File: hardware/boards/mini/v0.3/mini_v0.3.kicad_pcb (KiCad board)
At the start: 8 copper layers, 20 x 40 mm, 94 parts, among them IC1 NAU88C22YG, IC3 IS42S16160J-6BLI, J4 DF40C-90DP-0.4V, U1 W25Q128JVP, U2 LTV-217-G, U4 STM32H750XBHx, Y1 Crystal_GND24, Y3 32.768kHz

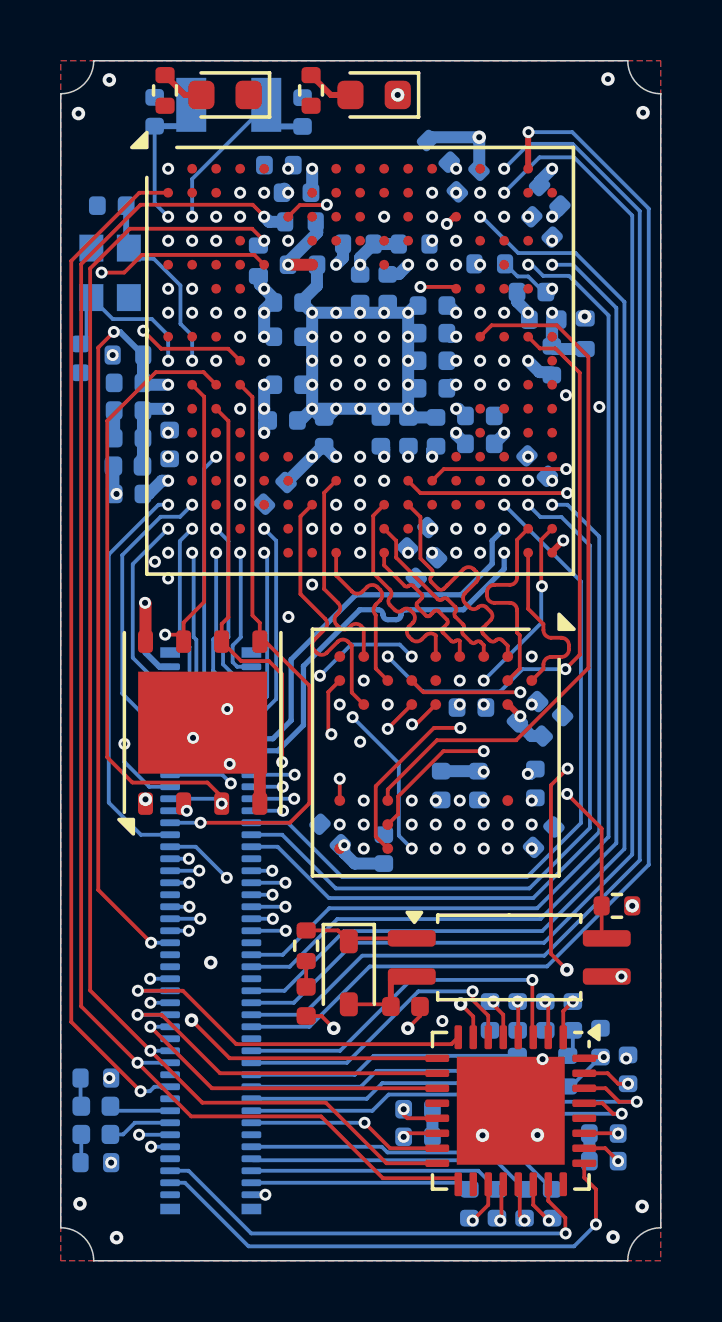
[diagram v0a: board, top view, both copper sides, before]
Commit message: mini: change flash to SOIC8 to fix routing
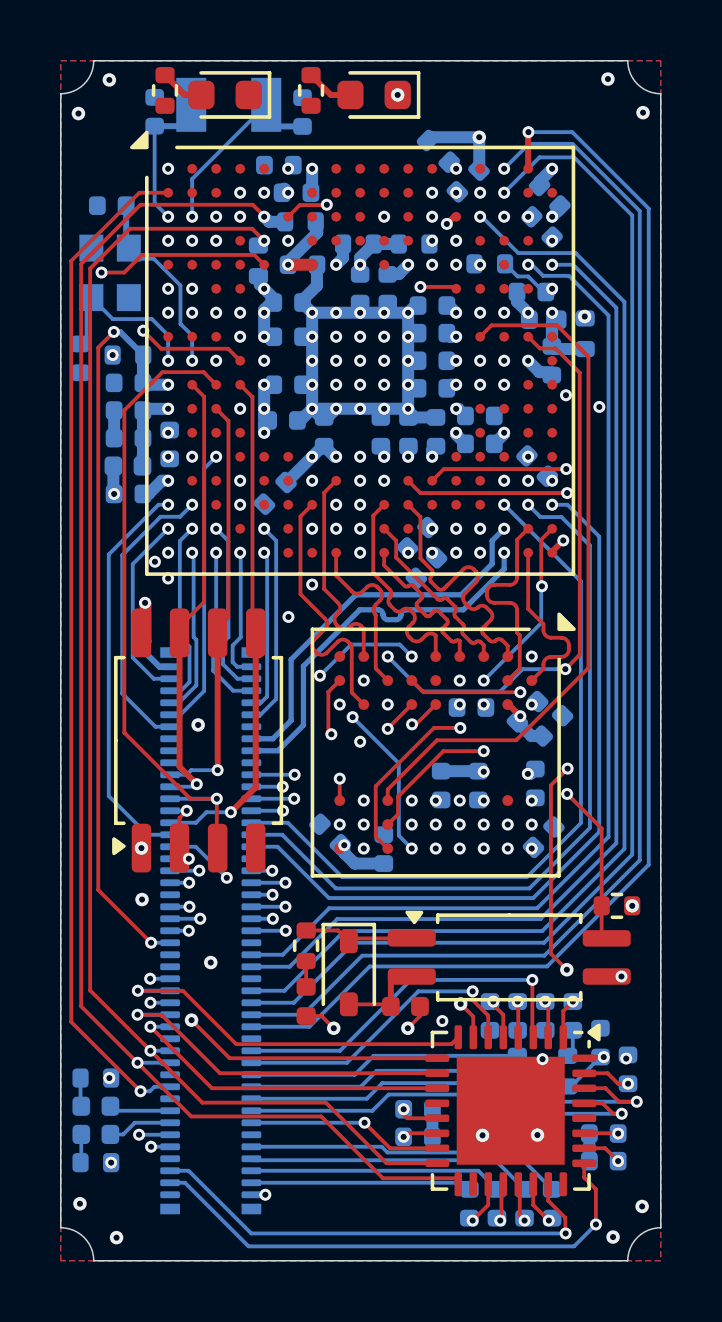
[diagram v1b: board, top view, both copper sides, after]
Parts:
- removed U1: W25Q128JVP, Package_SON:WSON-8-1EP_6x5mm_P1.27mm_EP3.4x4.3mm
- added U3: W25Q128JVS, Package_SO:SOIC-8_5.3x5.3mm_P1.27mm, F.Cu at (74.6, 79.7)
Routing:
- net GND: track 35.6 -> 31.8 mm, vias 73 -> 72
- net /QSPI_CLK: track 17.7 -> 14.3 mm, vias 2 -> 1
- net /QSPI_IO0: track 19.9 -> 17.1 mm
- net /QSPI_NCS: track 23.5 -> 25.1 mm
- net /QSPI_IO1: track 21.8 -> 23.1 mm
- net /QSPI_IO3: track 16.5 -> 15.5 mm, vias 2 -> 1

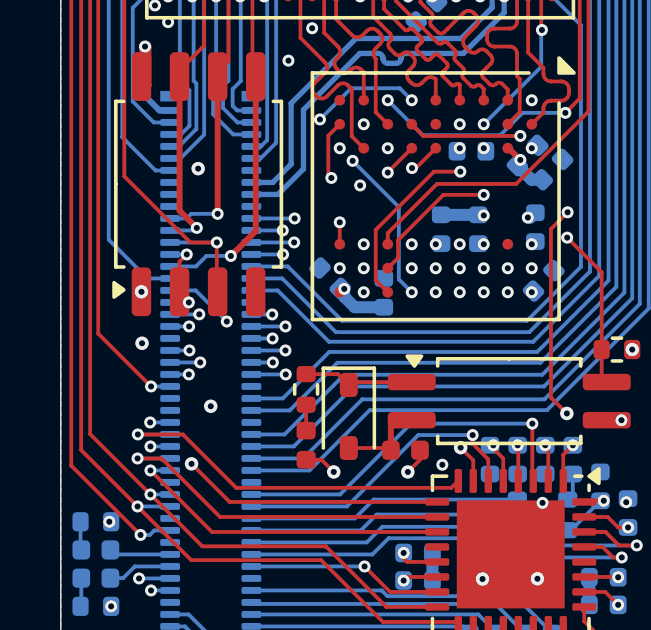
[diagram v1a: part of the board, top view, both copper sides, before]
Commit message: mini: more flash routing with new SOIC8 package
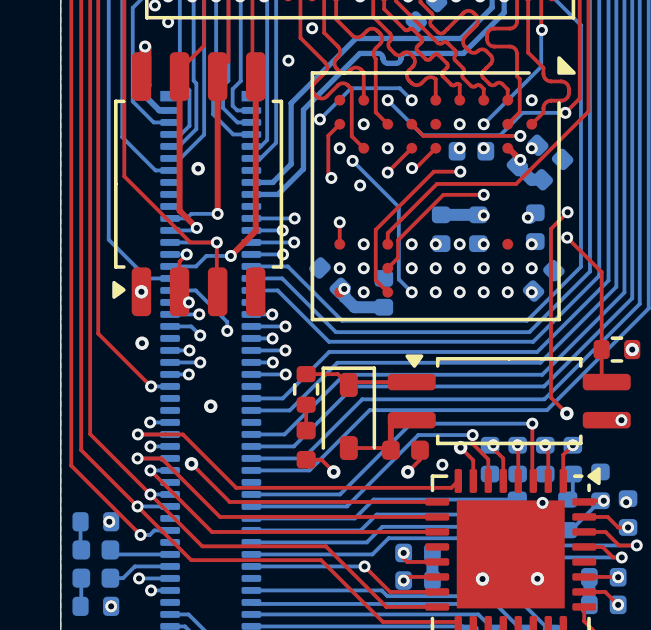
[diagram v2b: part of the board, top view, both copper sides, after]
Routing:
- net /QSPI_CS_EXP: track 36.3 -> 36.9 mm
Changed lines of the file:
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@@
 	)
 	(via
-		(at 74.28 84.4)
+		(at 74.65 84.7)
 		(size 0.4)
 		(drill 0.2)
@@
 	)
 	(segment
-		(start 73.645 84.4)
-		(end 74.28 84.4)
-		(width 0.127)
-		(layer "B.Cu")
+		(start 74.65 84.7)
+		(end 74.35 84.4)
+		(width 0.127)
+		(layer "B.Cu")
+		(net 206)
+	)
+	(segment
+		(start 74.35 84.4)
+		(end 73.645 84.4)
+		(width 0.127)
+		(layer "B.Cu")
+		(net 206)
+	)
+	(segment
+		(start 88.305 82.165)
+		(end 88.305 69.253876)
+		(width 0.127)
+		(layer "In3.Cu")
+		(net 206)
+	)
+	(segment
+		(start 85.81 84.66)
+		(end 88.305 82.165)
+		(width 0.127)
+		(layer "In3.Cu")
+		(net 206)
+	)
+	(segment
+		(start 78 83.34)
+		(end 79.32 84.66)
+		(width 0.127)
+		(layer "In3.Cu")
+		(net 206)
+	)
+	(segment
+		(start 88.3 69.248876)
+		(end 88.3 68.8865)
+		(width 0.127)
+		(layer "In3.Cu")
+		(net 206)
+	)
+	(segment
+		(start 88.3 68.8865)
+		(end 87.9535 68.54)
+		(width 0.127)
+		(layer "In3.Cu")
+		(net 206)
+	)
+	(segment
+		(start 76.06 83.34)
+		(end 78 83.34)
+		(width 0.127)
+		(layer "In3.Cu")
+		(net 206)
+	)
+	(segment
+		(start 79.32 84.66)
+		(end 85.81 84.66)
+		(width 0.127)
+		(layer "In3.Cu")
+		(net 206)
+	)
+	(segment
+		(start 74.72 84.63)
+		(end 74.77 84.63)
+		(width 0.127)
+		(layer "In3.Cu")
+		(net 206)
+	)
+	(segment
+		(start 74.77 84.63)
+		(end 76.06 83.34)
+		(width 0.127)
+		(layer "In3.Cu")
 		(net 206)
 	)
 	(segment
 		(start 88.305 69.253876)
-		(end 88.305 82.165)
-		(width 0.127)
-		(layer "In3.Cu")
-		(net 206)
-	)
-	(segment
-		(start 87.9535 68.54)
-		(end 88.3 68.8865)
-		(width 0.127)
-		(layer "In3.Cu")
-		(net 206)
-	)
-	(segment
-		(start 79.32 84.66)
-		(end 78 83.34)
-		(width 0.127)
-		(layer "In3.Cu")
-		(net 206)
-	)
-	(segment
-		(start 88.305 82.165)
-		(end 85.81 84.66)
-		(width 0.127)
-		(layer "In3.Cu")
-		(net 206)
-	)
-	(segment
-		(start 88.3 69.248876)
-		(end 88.305 69.253876)
-		(width 0.127)
-		(layer "In3.Cu")
-		(net 206)
-	)
-	(segment
-		(start 88.3 68.8865)
 		(end 88.3 69.248876)
 		(width 0.127)
@@
 	)
 	(segment
-		(start 85.81 84.66)
-		(end 79.32 84.66)
-		(width 0.127)
-		(layer "In3.Cu")
-		(net 206)
-	)
-	(segment
-		(start 78 83.34)
-		(end 75.83 83.34)
-		(width 0.127)
-		(layer "In3.Cu")
-		(net 206)
-	)
-	(segment
-		(start 74.77 84.4)
-		(end 74.28 84.4)
-		(width 0.127)
-		(layer "In3.Cu")
-		(net 206)
-	)
-	(segment
-		(start 75.83 83.34)
-		(end 74.77 84.4)
+		(start 74.65 84.7)
+		(end 74.72 84.63)
 		(width 0.127)
 		(layer "In3.Cu")
@@
 	)
 	(via
-		(at 75.535 84.235)
+		(at 75.55 84.55)
 		(size 0.4)
 		(drill 0.2)
@@
 	)
 	(segment
-		(start 75.535 84.235)
-		(end 74.5 83.2)
-		(width 0.127)
-		(layer "B.Cu")
-		(net 212)
-	)
-	(segment
 		(start 74.5 83.2)
 		(end 73.645 83.2)
@@
 	)
 	(segment
+		(start 75.55 84.55)
+		(end 75.55 84.25)
+		(width 0.127)
+		(layer "B.Cu")
+		(net 212)
+	)
+	(segment
+		(start 75.55 84.25)
+		(end 74.5 83.2)
+		(width 0.127)
+		(layer "B.Cu")
+		(net 212)
+	)
+	(segment
+		(start 76.135 83.635)
+		(end 77.825 83.635)
+		(width 0.127)
+		(layer "In3.Cu")
+		(net 212)
+	)
+	(segment
+		(start 86.73 66.59)
+		(end 85.97 66.59)
+		(width 0.127)
+		(layer "In3.Cu")
+		(net 212)
+	)
+	(segment
+		(start 85.97 66.59)
+		(end 84.78 65.4)
+		(width 0.127)
+		(layer "In3.Cu")
+		(net 212)
+	)
+	(segment
+		(start 79.15 84.96)
+		(end 86.14 84.96)
+		(width 0.127)
+		(layer "In3.Cu")
+		(net 212)
+	)
+	(segment
+		(start 75.55 84.22)
+		(end 76.135 83.635)
+		(width 0.127)
+		(layer "In3.Cu")
+		(net 212)
+	)
+	(segment
+		(start 75.55 84.55)
+		(end 75.55 84.22)
+		(width 0.127)
+		(layer "In3.Cu")
+		(net 212)
+	)
+	(segment
+		(start 88.58 82.52)
+		(end 88.58 68.44)
+		(width 0.127)
+		(layer "In3.Cu")
+		(net 212)
+	)
+	(segment
 		(start 86.14 84.96)
 		(end 88.58 82.52)
@@
 	)
 	(segment
-		(start 86.73 66.59)
-		(end 85.97 66.59)
-		(width 0.127)
-		(layer "In3.Cu")
-		(net 212)
-	)
-	(segment
 		(start 77.825 83.635)
 		(end 79.15 84.96)
@@
 	)
 	(segment
-		(start 76.135 83.635)
-		(end 77.825 83.635)
-		(width 0.127)
-		(layer "In3.Cu")
-		(net 212)
-	)
-	(segment
-		(start 75.535 84.235)
-		(end 76.135 83.635)
-		(width 0.127)
-		(layer "In3.Cu")
-		(net 212)
-	)
-	(segment
-		(start 79.15 84.96)
-		(end 86.14 84.96)
-		(width 0.127)
-		(layer "In3.Cu")
-		(net 212)
-	)
-	(segment
-		(start 88.58 82.52)
-		(end 88.58 68.44)
-		(width 0.127)
-		(layer "In3.Cu")
-		(net 212)
-	)
-	(segment
 		(start 88.58 68.44)
 		(end 86.73 66.59)
 		(width 0.127)
 		(layer "In3.Cu")
-		(net 212)
-	)
-	(segment
-		(start 85.97 66.59)
-		(end 84.78 65.4)
-		(width 0.127)
-		(layer "In3.Cu")
